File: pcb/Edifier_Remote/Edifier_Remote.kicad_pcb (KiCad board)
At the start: 2 copper layers, 4 parts, among them Q1 Q_NPN_BCE

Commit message: arange components
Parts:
- moved IR_Recv1 65.0 mm to (107.0, 133.8)
- moved Q1 45.9 mm to (117.7, 116.1)
- moved D1 0.68 mm to (132.0, 135.0)
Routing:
- net /3V3: track 0.00 -> 52.8 mm
- net Net-(D1-Pad1): track 0.00 -> 23.8 mm
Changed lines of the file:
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@@
     (thickness 1.6)
     (drawings 0)
-    (tracks 0)
+    (tracks 7)
     (zones 0)
     (modules 4)
@@
     (solder_mask_min_width 0.25)
     (aux_axis_origin 0 0)
-    (visible_elements FFFFFF7F)
+    (visible_elements 7FFFFFFF)
     (pcbplotparams
       (layerselection 0x010fc_ffffffff)
@@
   )
   (module Package_TO_SOT_THT:TO-220-3_Vertical (layer F.Cu)
-    (at 126.746 71.12)
+    (at 117.6655 116.1415)
     (descr "TO-220-3, Vertical, RM 2.54mm, see https://www.vishay.com/docs/66542/to-220-1.pdf")
     (tags "TO-220-3 Vertical RM 2.54mm")
@@
   )
   (module OptoDevice:Vishay_MOLD-3Pin (layer F.Cu)
-    (at 106.299 68.834)
+    (at 106.9975 133.7945)
     (descr "IR Receiver Vishay TSOP-xxxx, MOLD package, see https://www.vishay.com/docs/82669/tsop32s40f.pdf")
     (tags "IR Receiver Vishay TSOP-xxxx MOLD")
@@
   (module ESP32-DEVKITC-32D:MODULE_ESP32-DEVKITC-32D (layer F.Cu)
     (at 119.797 103.398)
-    (fp_text reference ESP32 (at -11.4644 -28.446) (layer F.SilkS)
+    (fp_text reference ESP32 (at -0.8615 -23.007) (layer F.SilkS)
       (effects (font (size 1.00039 1.00039) (thickness 0.05)))
     )
-    (fp_text value ESP32-DEVKITC-32D (at -10.8363 28.2945) (layer F.SilkS)
+    (fp_text value ESP32-DEVKITC-32D (at 0.218 -10.7515) (layer F.SilkS)
       (effects (font (size 1.00105 1.00105) (thickness 0.05)))
     )
@@
   )
   (module LED_THT:LED_D5.0mm (layer F.Cu)
-    (at 132.6515 135.255 180)
+    (at 132.0165 135.001 180)
     (descr "LED, diameter 5.0mm, 2 pins, http://cdn-reichelt.de/documents/datenblatt/A500/LL-504BC2E-009.pdf")
     (tags "LED diameter 5.0mm 2 pins")
@@
     )
   )
+  (segment (start 120.2055 117.3915) (end 120.2055 116.1415) (width 0.25) (layer F.Cu) (net 2))
+  (segment (start 120.2055 118.701902) (end 120.2055 117.3915) (width 0.25) (layer F.Cu) (net 2))
+  (segment (start 132.0165 130.512902) (end 120.2055 118.701902) (width 0.25) (layer F.Cu) (net 2))
+  (segment (start 132.0165 135.001) (end 132.0165 130.512902) (width 0.25) (layer F.Cu) (net 2))
+  (segment (start 108.127 83.638) (end 107.097 83.638) (width 0.25) (layer F.Cu) (net 39))
+  (segment (start 112.0775 87.5885) (end 108.127 83.638) (width 0.25) (layer F.Cu) (net 39))
+  (segment (start 112.0775 133.7945) (end 112.0775 87.5885) (width 0.25) (layer F.Cu) (net 39))
 )

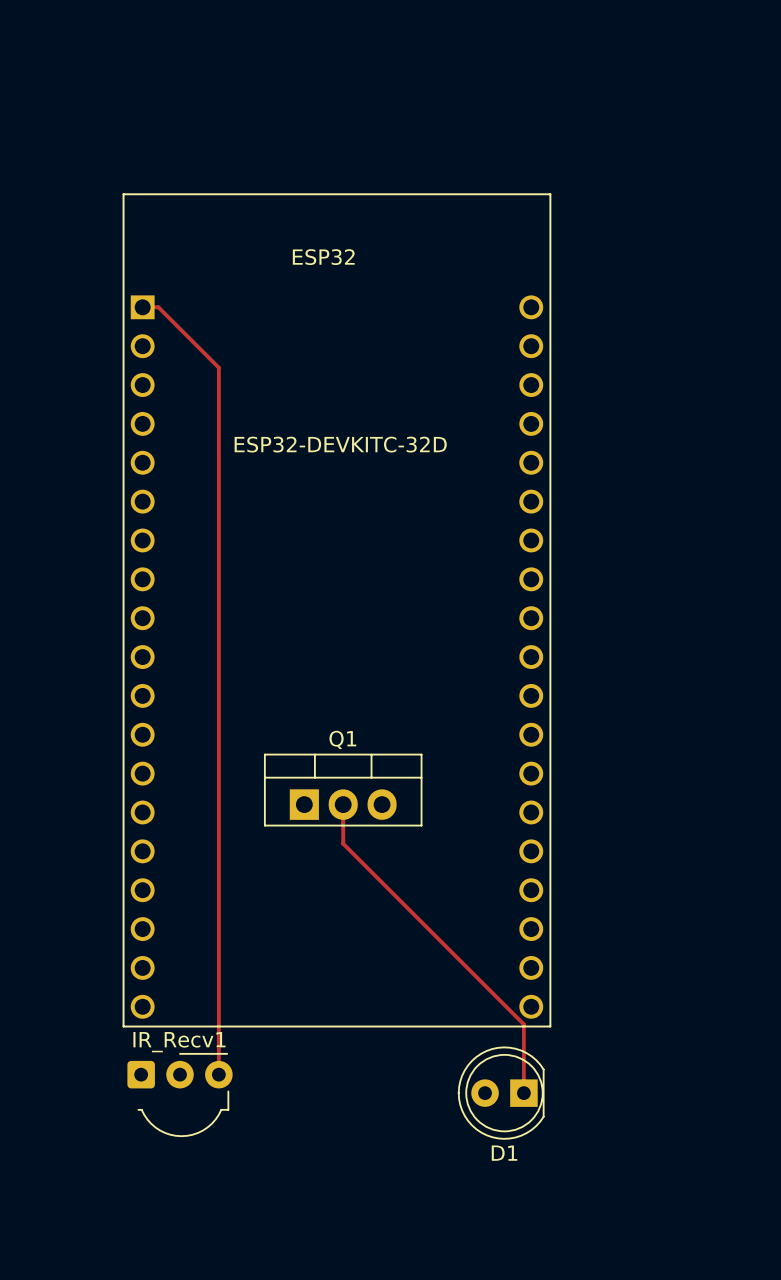
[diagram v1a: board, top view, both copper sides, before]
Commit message: add logo
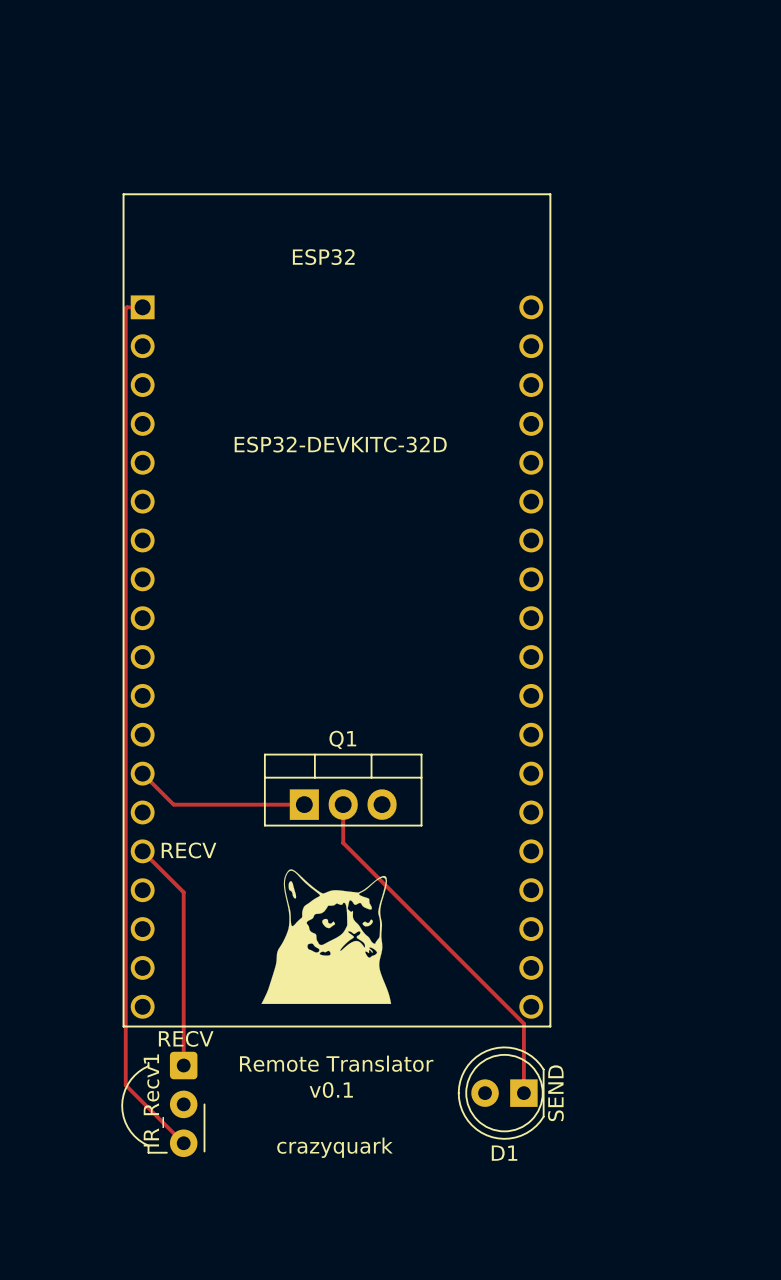
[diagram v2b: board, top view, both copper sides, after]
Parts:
- added G***: LOGO, Logo:Logo, F.Cu at (119.1, 124.4)
- added LOGO: LOGO, Logo:Logo, B.Cu at (119.2, 102.9)
- moved IR_Recv1 2.84 mm to (109.8, 133.2), turned to 270 degrees
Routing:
- net /RECV: track 0.00 -> 15.1 mm
- net /SEND: track 0.00 -> 11.4 mm
- net /3V3: track 52.8 -> 57.3 mm
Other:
- board text added: "RECV"
- board text added: "Remote Translator"
- board text added: "Remote Translator v0.1"
- board text added: "SEND"
- board text added: "crazyquark"
- board text added: "v0.1"
- board text added: "www.cristiansandu.ro"

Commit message: add filled zones
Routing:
- net GND: track 0.00 -> 4.35 mm
- added copper zone on B.Cu, net /5V
- added copper zone on F.Cu, net GND
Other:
- board outline added: 29.2 x 64.8 mm
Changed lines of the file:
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@@
   (general
     (thickness 1.6)
-    (drawings 8)
-    (tracks 12)
+    (drawings 12)
+    (tracks 15)
     (zones 0)
     (modules 6)
@@
     )
   )
+  (gr_line (start 105.156 75.438) (end 105.156 140.208) (layer Edge.Cuts) (width 0.1))
+  (gr_line (start 134.366 75.438) (end 105.156 75.438) (layer Edge.Cuts) (width 0.1))
+  (gr_line (start 134.366 140.208) (end 134.366 75.438) (layer Edge.Cuts) (width 0.1))
+  (gr_line (start 105.156 140.208) (end 134.366 140.208) (layer Edge.Cuts) (width 0.1))
   (gr_text crazyquark (at 119.63146 138.48588) (layer F.SilkS)
     (effects (font (size 1 1) (thickness 0.15)))
@@
   (segment (start 109.7788 121.8798) (end 107.097 119.198) (width 0.25) (layer F.Cu) (net 25))
   (segment (start 109.7788 133.1976) (end 109.7788 121.8798) (width 0.25) (layer F.Cu) (net 25))
+  (segment (start 122.67049 114.81649) (end 119.676339 114.81649) (width 0.25) (layer F.Cu) (net 26))
+  (segment (start 122.7455 116.1415) (end 122.7455 114.8915) (width 0.25) (layer F.Cu) (net 26))
+  (segment (start 122.7455 114.8915) (end 122.67049 114.81649) (width 0.25) (layer F.Cu) (net 26))
   (segment (start 109.1205 116.1415) (end 107.097 114.118) (width 0.25) (layer F.Cu) (net 27))
   (segment (start 117.6655 116.1415) (end 109.1205 116.1415) (width 0.25) (layer F.Cu) (net 27))
@@
   (segment (start 105.991999 134.490799) (end 105.991999 83.713001) (width 0.25) (layer F.Cu) (net 39))
   (segment (start 109.7788 138.2776) (end 105.991999 134.490799) (width 0.25) (layer F.Cu) (net 39))
+  (zone (net 26) (net_name GND) (layer F.Cu) (hatch edge 0.508)
+    (connect_pads (clearance 0.508))
+    (min_thickness 0.254)
+    (fill yes (arc_segments 32) (thermal_gap 0.508) (thermal_bridge_width 0.508))
+    (polygon
+      (pts
+        (xy 103.886 73.406) (xy 136.906 73.406) (xy 136.906 142.494) (xy 103.632 142.494)
+      )
+    )
+  )
+  (zone (net 1) (net_name /5V) (layer B.Cu) (hatch edge 0.508)
+    (connect_pads (clearance 0.508))
+    (min_thickness 0.254)
+    (fill yes (arc_segments 32) (thermal_gap 0.508) (thermal_bridge_width 0.508))
+    (polygon
+      (pts
+        (xy 103.886 72.644) (xy 137.16 72.644) (xy 137.16 144.78) (xy 103.886 144.78)
+      )
+    )
+  )
 )

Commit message: pcb
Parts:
- added 1: MountingHole_3.2mm_M3, MountingHole:MountingHole_3.2mm_M3, F.Cu at (120.4, 136.1)
- added 2: MountingHole_3.2mm_M3, MountingHole:MountingHole_3.2mm_M3, F.Cu at (109.7, 79.5)
- added 3: MountingHole_3.2mm_M3, MountingHole:MountingHole_3.2mm_M3, F.Cu at (130.3, 79.5)
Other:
- board text removed: "crazyquark"
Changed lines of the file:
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@@
   (general
     (thickness 1.6)
-    (drawings 12)
+    (drawings 11)
     (tracks 15)
     (zones 0)
-    (modules 6)
+    (modules 9)
     (nets 40)
   )
   (page A4)
   (layers
-    (0 F.Cu signal)
-    (31 B.Cu signal)
-    (32 B.Adhes user)
-    (33 F.Adhes user)
-    (34 B.Paste user)
-    (35 F.Paste user)
-    (36 B.SilkS user)
+    (0 F.Cu signal hide)
+    (31 B.Cu signal hide)
+    (32 B.Adhes user hide)
+    (33 F.Adhes user hide)
+    (34 B.Paste user hide)
+    (35 F.Paste user hide)
+    (36 B.SilkS user hide)
     (37 F.SilkS user)
-    (38 B.Mask user)
-    (39 F.Mask user)
-    (40 Dwgs.User user)
-    (41 Cmts.User user)
-    (42 Eco1.User user)
-    (43 Eco2.User user)
-    (44 Edge.Cuts user)
-    (45 Margin user)
-    (46 B.CrtYd user)
-    (47 F.CrtYd user)
-    (48 B.Fab user)
-    (49 F.Fab user)
+    (38 B.Mask user hide)
+    (39 F.Mask user hide)
+    (40 Dwgs.User user hide)
+    (41 Cmts.User user hide)
+    (42 Eco1.User user hide)
+    (43 Eco2.User user hide)
+    (44 Edge.Cuts user hide)
+    (45 Margin user hide)
+    (46 B.CrtYd user hide)
+    (47 F.CrtYd user hide)
+    (48 B.Fab user hide)
+    (49 F.Fab user hide)
   )
   (setup
@@
     (add_net "Net-(ESP32-Pad8)")
     (add_net "Net-(ESP32-Pad9)")
+  )
+  (module MountingHole:MountingHole_3.2mm_M3 (layer F.Cu)
+    (at 120.396 136.144)
+    (descr "Mounting Hole 3.2mm, no annular, M3")
+    (tags "mounting hole 3.2mm no annular m3")
+    (attr virtual)
+    (fp_text reference 1 (at 3.302 0) (layer F.SilkS)
+      (effects (font (size 1 1) (thickness 0.15)))
+    )
+    (fp_text value MountingHole_3.2mm_M3 (at 0 4.2) (layer F.Fab)
+      (effects (font (size 1 1) (thickness 0.15)))
+    )
+    (fp_circle (center 0 0) (end 3.45 0) (layer F.CrtYd) (width 0.05))
+    (fp_circle (center 0 0) (end 3.2 0) (layer Cmts.User) (width 0.15))
+    (fp_text user %R (at 0.3 0) (layer F.Fab)
+      (effects (font (size 1 1) (thickness 0.15)))
+    )
+    (pad 1 np_thru_hole circle (at 0 0) (size 3.2 3.2) (drill 3.2) (layers *.Cu *.Mask))
+  )
+  (module MountingHole:MountingHole_3.2mm_M3 (layer F.Cu)
+    (at 130.302 79.502)
+    (descr "Mounting Hole 3.2mm, no annular, M3")
+    (tags "mounting hole 3.2mm no annular m3")
+    (attr virtual)
+    (fp_text reference 3 (at 2.794 -1.016) (layer F.SilkS)
+      (effects (font (size 1 1) (thickness 0.15)))
+    )
+    (fp_text value MountingHole_3.2mm_M3 (at 0 4.2) (layer F.Fab)
+      (effects (font (size 1 1) (thickness 0.15)))
+    )
+    (fp_circle (center 0 0) (end 3.45 0) (layer F.CrtYd) (width 0.05))
+    (fp_circle (center 0 0) (end 3.2 0) (layer Cmts.User) (width 0.15))
+    (fp_text user %R (at 0.3 0) (layer F.Fab)
+      (effects (font (size 1 1) (thickness 0.15)))
+    )
+    (pad 1 np_thru_hole circle (at 0 0) (size 3.2 3.2) (drill 3.2) (layers *.Cu *.Mask))
+  )
+  (module MountingHole:MountingHole_3.2mm_M3 (layer F.Cu)
+    (at 109.728 79.502)
+    (descr "Mounting Hole 3.2mm, no annular, M3")
+    (tags "mounting hole 3.2mm no annular m3")
+    (attr virtual)
+    (fp_text reference 2 (at -2.54 -1.016) (layer F.SilkS)
+      (effects (font (size 1 1) (thickness 0.15)))
+    )
+    (fp_text value MountingHole_3.2mm_M3 (at 0 4.2) (layer F.Fab)
+      (effects (font (size 1 1) (thickness 0.15)))
+    )
+    (fp_circle (center 0 0) (end 3.45 0) (layer F.CrtYd) (width 0.05))
+    (fp_circle (center 0 0) (end 3.2 0) (layer Cmts.User) (width 0.15))
+    (fp_text user %R (at 0.3 0) (layer F.Fab)
+      (effects (font (size 1 1) (thickness 0.15)))
+    )
+    (pad 1 np_thru_hole circle (at 0 0) (size 3.2 3.2) (drill 3.2) (layers *.Cu *.Mask))
   )
   (module Logo:Logo (layer F.Cu)
@@
     )
   )
+  (gr_text v0.1 (at 114.554 136.144) (layer F.SilkS)
+    (effects (font (size 1 1) (thickness 0.25)))
+  )
   (gr_line (start 105.156 75.438) (end 105.156 140.208) (layer Edge.Cuts) (width 0.1))
   (gr_line (start 134.366 75.438) (end 105.156 75.438) (layer Edge.Cuts) (width 0.1))
   (gr_line (start 134.366 140.208) (end 134.366 75.438) (layer Edge.Cuts) (width 0.1))
   (gr_line (start 105.156 140.208) (end 134.366 140.208) (layer Edge.Cuts) (width 0.1))
-  (gr_text crazyquark (at 119.63146 138.48588) (layer F.SilkS)
-    (effects (font (size 1 1) (thickness 0.15)))
-  )
-  (gr_text v0.1 (at 119.4689 134.83336) (layer F.SilkS)
-    (effects (font (size 1 1) (thickness 0.15)))
-  )
   (gr_text "Remote Translator" (at 119.71274 133.12902) (layer F.SilkS)
     (effects (font (size 1 1) (thickness 0.15)))

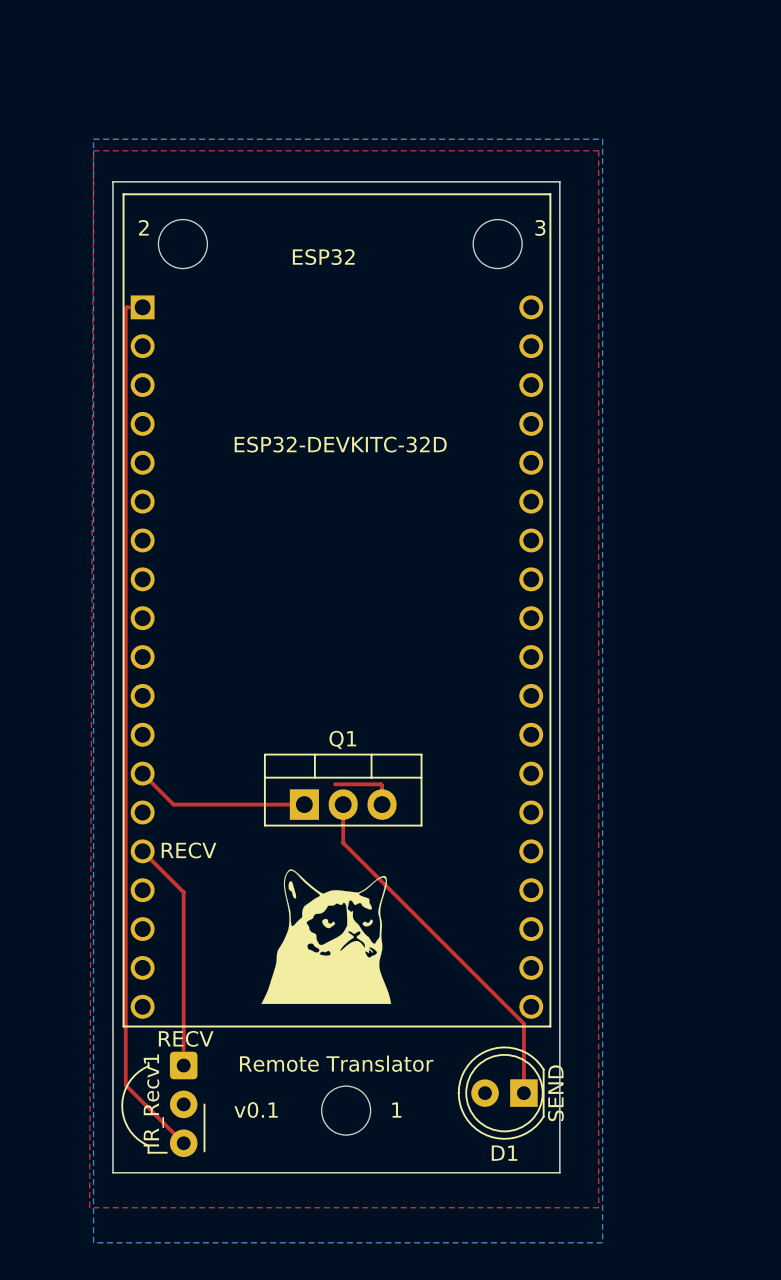
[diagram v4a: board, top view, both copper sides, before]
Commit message: replace w/ esp 32 doit
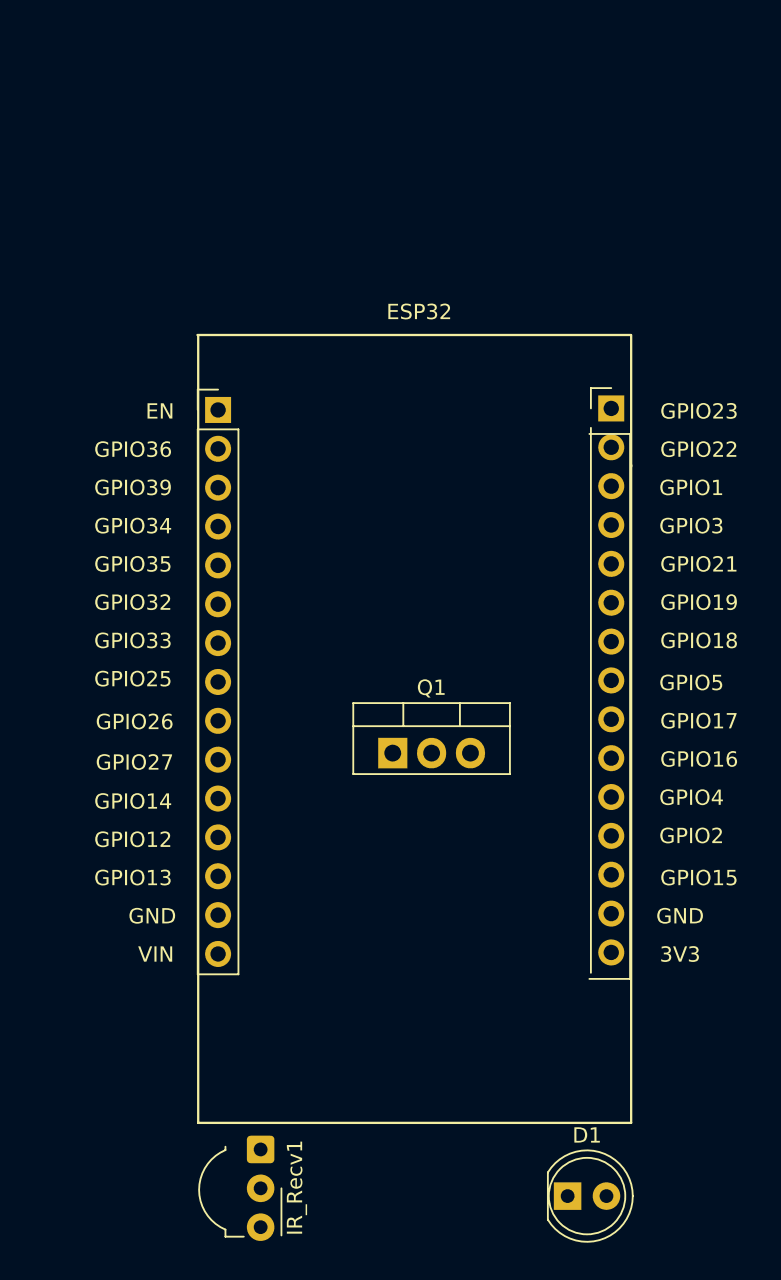
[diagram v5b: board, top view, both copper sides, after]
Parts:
- removed 1, 2, 3: MountingHole_3.2mm_M3, MountingHole:MountingHole_3.2mm_M3
- removed G***, LOGO: LOGO, Logo:Logo
- ESP32: value ESP32-DEVKITC-32D -> ESP32_Devkit_DOIT_V1; footprint ESP32-DEVKITC-32D:MODULE_ESP32-DEVKITC-32D -> ESP32:ESP32_Devkit_DOIT_V1
- moved ESP32 34.8 mm to (110.7, 136.9)
- moved IR_Recv1 7.44 mm to (114.8, 138.7)
- moved D1 7.31 mm to (134.9, 141.7), turned to 0 degrees
- moved Q1 6.69 mm to (123.4, 112.8)
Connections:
- ESP32 pad 1: /3V3 -> Net-(ESP32-Pad1)
- ESP32 pad 10: Net-(ESP32-Pad10) -> GND
- ESP32 pad 11: Net-(ESP32-Pad11) -> /RECV
- ESP32 pad 13: /SEND -> Net-(ESP32-Pad13)
- ESP32 pad 14: GND -> Net-(ESP32-Pad14)
- ESP32 pad 15: /RECV -> /5V
- ESP32 pad 19: /5V -> Net-(ESP32-Pad19)
- ESP32 pad 9: Net-(ESP32-Pad9) -> /SEND
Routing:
- net /3V3: track 57.3 -> 0.00 mm
- net Net-(D1-Pad1): track 23.8 -> 0.00 mm
- net /RECV: track 15.1 -> 0.00 mm
- net /SEND: track 11.4 -> 0.00 mm
- net GND: track 4.35 -> 0.00 mm
- removed copper zone on B.Cu, net /5V
- removed copper zone on F.Cu, net GND
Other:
- board outline removed
- rule pad_to_mask_clearance: 0.051 -> 0
- board text removed: "RECV"
- board text removed: "Remote Translator"
- board text removed: "Remote Translator v0.1"
- board text removed: "SEND"
- board text removed: "v0.1"
- board text removed: "www.cristiansandu.ro"

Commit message: update wires
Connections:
- ESP32 pad 10: GND -> Net-(ESP32-Pad10)
- ESP32 pad 11: /RECV -> Net-(ESP32-Pad11)
- ESP32 pad 12: Net-(ESP32-Pad12) -> /SEND
- ESP32 pad 13: Net-(ESP32-Pad13) -> /RECV
- ESP32 pad 14: Net-(ESP32-Pad14) -> GND
- ESP32 pad 16: Net-(ESP32-Pad16) -> /3V3
- ESP32 pad 9: /SEND -> Net-(ESP32-Pad9)

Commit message: finished board design
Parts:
- removed ESP32: ESP32_Devkit_DOIT_V1, ESP32:ESP32_Devkit_DOIT_V1
- added 1: MountingHole_3.2mm_M3, MountingHole:MountingHole_3.2mm_M3, F.Cu at (105.0, 70.3)
- added 2: MountingHole_3.2mm_M3, MountingHole:MountingHole_3.2mm_M3, F.Cu at (130.0, 70.2)
- added 3: MountingHole_3.2mm_M3, MountingHole:MountingHole_3.2mm_M3, F.Cu at (117.5, 132.3)
- added CUT: BoardCutout, ESP32:BoardCutout, F.Cu at (117.3, 98.3)
- added G***: LOGO, Logo:Logo, B.Cu at (117.0, 83.4)
- added U1: ESP32_DevKit, ESP32:ESP32_DevKit_36PIN, F.Cu at (114.9, 80.1)
- moved D1 15.5 mm to (126.6, 128.7), turned to 180 degrees
- moved IR_Recv1 13.6 mm to (110.1, 125.9)
- moved Q1 2.88 mm to (120.6, 112.5), turned to 180 degrees
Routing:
- net Net-(D1-Pad1): track 0.00 -> 35.3 mm
- net /3V3: track 0.00 -> 29.3 mm
- net /RECV: track 0.00 -> 25.4 mm
- net /SEND: track 0.00 -> 21.3 mm
- added copper zone on B.Cu, net /5V
- added copper zone on F.Cu, net GND
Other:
- board outline added: 33 x 70 mm
- board text added: "Remote Translator v0.1"
- board text added: "cristiansandu.ro"
